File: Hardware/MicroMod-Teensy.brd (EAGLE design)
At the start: 22 x 22.8 mm, 80 parts, among them J1 MICROMOD-2222, Q1 20V/4.2A/52mΩ/1.4W, Q2 20V/0.2A/8MHz/1.2Ω/1Vth, U1 IMXRT1062DV10X10, U3 MKL02Z32VFG4, U4 W25QXX128MBIT-6X5, Y1 32.768kHz, Y2 24MHz

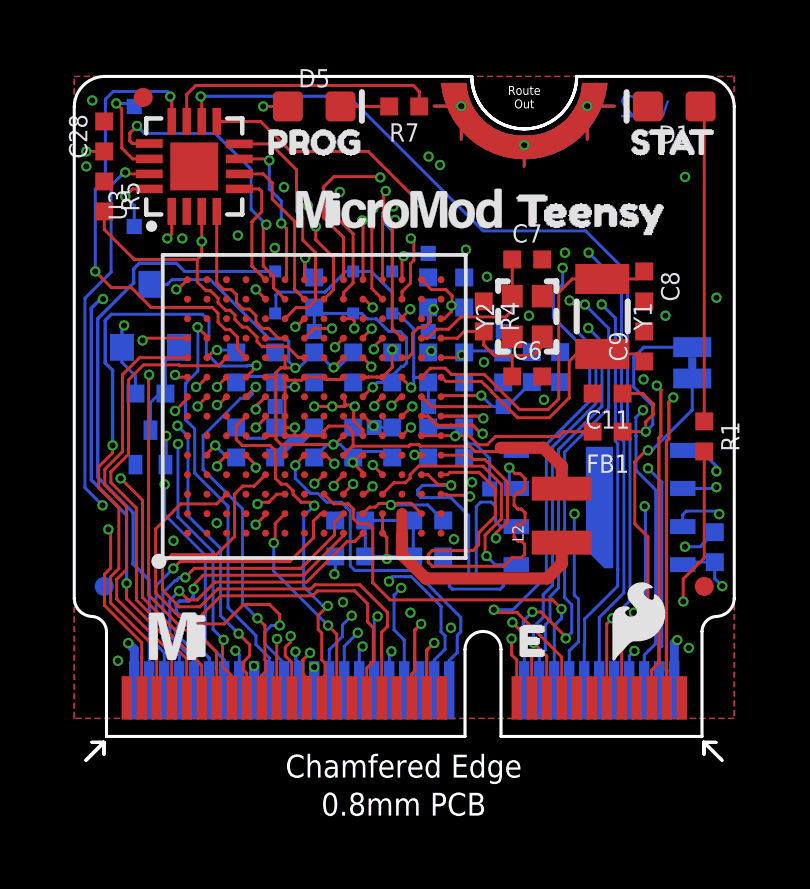
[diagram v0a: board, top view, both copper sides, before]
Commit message: Fix DAT2/DAT3, now correctly connected to B0_04 and B0_05.
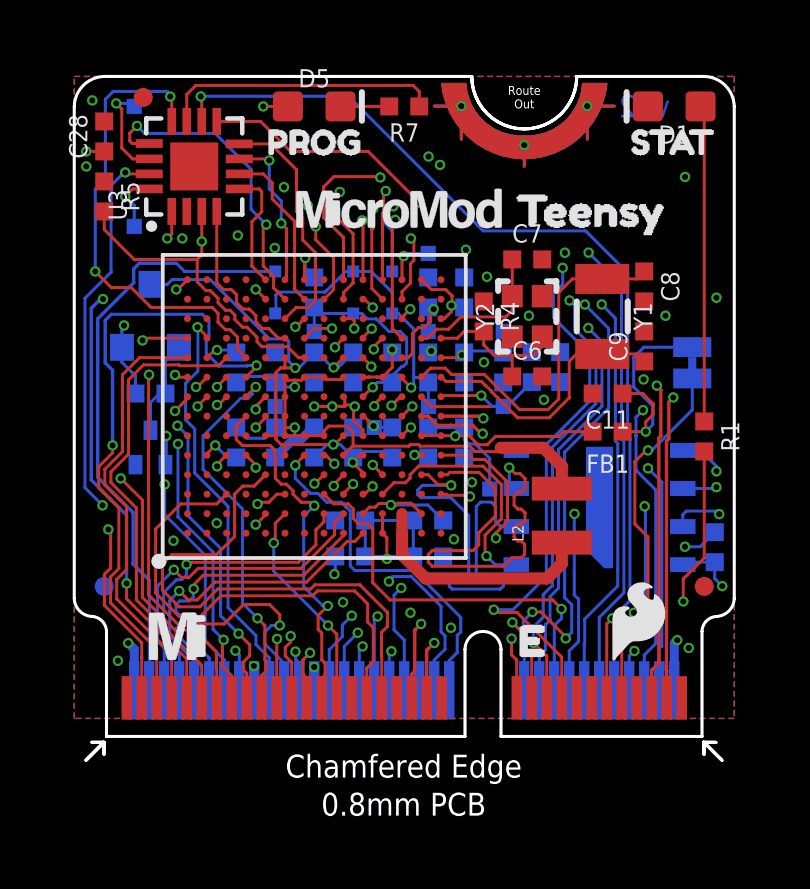
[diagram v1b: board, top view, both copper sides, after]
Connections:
- removed net 38/DAT3: J1.70, U1.H2
- removed net 39/DAT2: J1.68, U1.J2
- new net 38/DAT2: J1.68, U1.H2
- new net 39/DAT3: J1.70, U1.J2
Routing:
- net 39/DAT3: track 0.00 -> 11.2 mm, vias 0 -> 1
- net 39/DAT2: track 10.8 -> 0.00 mm, vias 1 -> 0
- net 38/DAT2: track 0.00 -> 10.6 mm, vias 0 -> 1
- net 38/DAT3: track 10.5 -> 0.00 mm, vias 1 -> 0
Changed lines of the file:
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@@
 <?xml version="1.0" encoding="utf-8"?>
 <!DOCTYPE eagle SYSTEM "eagle.dtd">
-<eagle version="9.6.0">
+<eagle version="9.6.2">
 <drawing>
 <settings>
@@
 <layer number="19" name="Unrouted" color="6" fill="1" visible="yes" active="yes"/>
 <layer number="20" name="Dimension" color="24" fill="1" visible="yes" active="yes"/>
-<layer number="21" name="tPlace" color="16" fill="1" visible="yes" active="yes"/>
+<layer number="21" name="tPlace" color="16" fill="1" visible="no" active="yes"/>
 <layer number="22" name="bPlace" color="14" fill="1" visible="yes" active="yes"/>
 <layer number="23" name="tOrigins" color="15" fill="1" visible="yes" active="yes"/>
@@
 <layer number="47" name="Measures" color="7" fill="1" visible="no" active="yes"/>
 <layer number="48" name="Document" color="7" fill="1" visible="no" active="yes"/>
-<layer number="49" name="Reference" color="7" fill="1" visible="no" active="yes"/>
+<layer number="49" name="Reference" color="7" fill="1" visible="yes" active="yes"/>
 <layer number="50" name="dxf" color="7" fill="1" visible="no" active="yes"/>
 <layer number="51" name="tDocu" color="6" fill="1" visible="yes" active="yes"/>
@@
 <wire x1="4.3" y1="5.36375" x2="7.65109375" y2="5.36375" width="0.1016" layer="1"/>
 <wire x1="7.65109375" y1="5.36375" x2="8.975" y2="6.68765625" width="0.1016" layer="1"/>
-<wire x1="4.31" y1="2.79" x2="4.01964375" y2="2.79" width="0.1143" layer="16"/>
-<wire x1="3.39535" y1="3.57535" x2="3.51" y2="3.69" width="0.1143" layer="16"/>
-<wire x1="4.05695" y1="3.69" x2="4.15695" y2="3.79" width="0.1143" layer="16"/>
-<wire x1="4.15695" y1="3.79" x2="4.15695" y2="3.94" width="0.1143" layer="16"/>
-<wire x1="4.15695" y1="3.94" x2="4.05695" y2="4.04" width="0.1143" layer="16"/>
-<wire x1="3.49535" y1="4.04" x2="3.39535" y2="4.14" width="0.1143" layer="16"/>
-<wire x1="3.39535" y1="4.3904" x2="3.51" y2="4.50505" width="0.1143" layer="16"/>
-<wire x1="3.51" y1="4.50505" x2="3.83874375" y2="4.50505" width="0.1143" layer="16"/>
-<wire x1="3.968" y1="4.63430625" x2="3.968" y2="4.895775" width="0.1143" layer="16"/>
-<wire x1="3.968" y1="4.63430625" x2="3.83874375" y2="4.50505" width="0.1143" layer="16"/>
-<wire x1="4.5" y1="2.6" x2="4.31" y2="2.79" width="0.1143" layer="16"/>
-<wire x1="4.01964375" y1="2.79" x2="3.39535" y2="3.41429375" width="0.1143" layer="16"/>
-<wire x1="3.39535" y1="3.41429375" x2="3.39535" y2="3.57535" width="0.1143" layer="16"/>
-<wire x1="3.51" y1="3.69" x2="4.05695" y2="3.69" width="0.1143" layer="16"/>
-<wire x1="4.05695" y1="4.04" x2="3.49535" y2="4.04" width="0.1143" layer="16"/>
-<wire x1="3.39535" y1="4.14" x2="3.39535" y2="4.3904" width="0.1143" layer="16"/>
+<wire x1="4.31" y1="2.79" x2="4.01964375" y2="2.79" width="0.1016" layer="16"/>
+<wire x1="3.39535" y1="3.57535" x2="3.51" y2="3.69" width="0.1016" layer="16"/>
+<wire x1="4.05695" y1="3.69" x2="4.15695" y2="3.79" width="0.1016" layer="16"/>
+<wire x1="4.15695" y1="3.79" x2="4.15695" y2="3.94" width="0.1016" layer="16"/>
+<wire x1="4.15695" y1="3.94" x2="4.05695" y2="4.04" width="0.1016" layer="16"/>
+<wire x1="3.49535" y1="4.04" x2="3.39535" y2="4.14" width="0.1016" layer="16"/>
+<wire x1="3.39535" y1="4.3904" x2="3.51" y2="4.50505" width="0.1016" layer="16"/>
+<wire x1="3.51" y1="4.50505" x2="3.83874375" y2="4.50505" width="0.1016" layer="16"/>
+<wire x1="3.968" y1="4.63430625" x2="3.968" y2="4.895775" width="0.1016" layer="16"/>
+<wire x1="3.968" y1="4.63430625" x2="3.83874375" y2="4.50505" width="0.1016" layer="16"/>
+<wire x1="4.5" y1="2.6" x2="4.31" y2="2.79" width="0.1016" layer="16"/>
+<wire x1="4.01964375" y1="2.79" x2="3.39535" y2="3.41429375" width="0.1016" layer="16"/>
+<wire x1="3.39535" y1="3.41429375" x2="3.39535" y2="3.57535" width="0.1016" layer="16"/>
+<wire x1="3.51" y1="3.69" x2="4.05695" y2="3.69" width="0.1016" layer="16"/>
+<wire x1="4.05695" y1="4.04" x2="3.49535" y2="4.04" width="0.1016" layer="16"/>
+<wire x1="3.39535" y1="4.14" x2="3.39535" y2="4.3904" width="0.1016" layer="16"/>
 <contactref element="J1" pad="64"/>
 <wire x1="4.5" y1="1.525" x2="4.5" y2="2.6" width="0.1016" layer="16"/>
@@
 <wire x1="8.65" y1="8.34" x2="8.4011375" y2="8.0911375" width="0.1016" layer="2"/>
 </signal>
-<signal name="38/DAT3">
-<contactref element="U1" pad="H2"/>
-<wire x1="8.325" y1="7.415" x2="8.22095" y2="7.415" width="0.1016" layer="1"/>
-<wire x1="8.22095" y1="7.415" x2="7.97465" y2="7.1687" width="0.1016" layer="1"/>
-<wire x1="7.97465" y1="6.61205" x2="7.97465" y2="7.1687" width="0.1016" layer="1"/>
-<via x="3.3" y="5.59" extent="1-16" drill="0.2"/>
-<wire x1="7.97465" y1="6.61205" x2="7.18355" y2="5.82095" width="0.1016" layer="1"/>
-<wire x1="3.3" y1="5.59" x2="3.53095" y2="5.82095" width="0.1016" layer="1"/>
-<wire x1="3.53095" y1="5.82095" x2="7.18355" y2="5.82095" width="0.1016" layer="1"/>
-<wire x1="3" y1="2.79" x2="2.7286" y2="3.0614" width="0.1016" layer="16"/>
-<wire x1="2.7286" y1="5.0186" x2="3.3" y2="5.59" width="0.1016" layer="16"/>
-<wire x1="2.7286" y1="3.0614" x2="2.7286" y2="5.0186" width="0.1016" layer="16"/>
+<signal name="39/DAT3">
 <contactref element="J1" pad="70"/>
-<wire x1="3" y1="1.525" x2="3" y2="2.79" width="0.1016" layer="16"/>
-</signal>
-<signal name="39/DAT2">
 <contactref element="U1" pad="J2"/>
 <wire x1="8.975" y1="7.415" x2="8.67535" y2="7.11535" width="0.1016" layer="1"/>
 <wire x1="8.67535" y1="7.11535" x2="8.67535" y2="6.7113" width="0.1016" layer="1"/>
 <wire x1="8.67535" y1="6.7113" x2="7.5564" y2="5.59235" width="0.1016" layer="1"/>
-<via x="3.7" y="5.29" extent="1-16" drill="0.2"/>
-<wire x1="3.7" y1="5.29" x2="4.00235" y2="5.59235" width="0.1016" layer="1"/>
-<wire x1="4.00235" y1="5.59235" x2="7.5564" y2="5.59235" width="0.1016" layer="1"/>
-<wire x1="3.5" y1="2.69" x2="2.9572" y2="3.2328" width="0.1016" layer="16"/>
-<wire x1="3.358625" y1="5.1813" x2="3.3985" y2="5.1813" width="0.1016" layer="16"/>
-<wire x1="3.3985" y1="5.1813" x2="3.5072" y2="5.29" width="0.1016" layer="16"/>
-<wire x1="2.9572" y1="3.2328" x2="2.9572" y2="4.779875" width="0.1016" layer="16"/>
-<wire x1="2.9572" y1="4.779875" x2="3.358625" y2="5.1813" width="0.1016" layer="16"/>
-<wire x1="3.5072" y1="5.29" x2="3.7" y2="5.29" width="0.1016" layer="16"/>
-<contactref element="J1" pad="68"/>
-<wire x1="3.5" y1="1.525" x2="3.5" y2="2.69" width="0.1016" layer="16"/>
+<via x="3.319" y="5.544" extent="1-16" drill="0.2"/>
+<wire x1="4.12935" y1="5.59235" x2="3.827" y2="5.29" width="0.1016" layer="1"/>
+<wire x1="3.827" y1="5.29" x2="3.573" y2="5.29" width="0.1016" layer="1"/>
+<wire x1="3.319" y1="5.544" x2="3.573" y2="5.29" width="0.1016" layer="1"/>
+<wire x1="4.12935" y1="5.59235" x2="7.5564" y2="5.59235" width="0.1016" layer="1"/>
+<wire x1="3" y1="1.525" x2="3" y2="2.93855625" width="0.1016" layer="16"/>
+<wire x1="3" y1="2.93855625" x2="2.7794" y2="3.15915625" width="0.1016" layer="16"/>
+<wire x1="2.7794" y1="3.15915625" x2="2.7794" y2="5.0044" width="0.1016" layer="16"/>
+<wire x1="2.7794" y1="5.0044" x2="3.319" y2="5.544" width="0.1016" layer="16"/>
 </signal>
 <signal name="N$31">
@@
 <wire x1="11.72218125" y1="9.7477" x2="12.4875875" y2="9.7477" width="0.1016" layer="2"/>
 </signal>
+<signal name="38/DAT2">
+<contactref element="U1" pad="H2"/>
+<contactref element="J1" pad="68"/>
+<wire x1="8.325" y1="7.415" x2="8.325" y2="7.1459875" width="0.1016" layer="1"/>
+<wire x1="8.0556" y1="6.37891875" x2="7.47223125" y2="5.79555" width="0.1016" layer="1"/>
+<wire x1="8.325" y1="7.1459875" x2="8.0556" y2="6.8765875" width="0.1016" layer="1"/>
+<wire x1="8.0556" y1="6.8765875" x2="8.0556" y2="6.37891875" width="0.1016" layer="1"/>
+<via x="3.74289375" y="5.72095" extent="1-16" drill="0.2"/>
+<wire x1="7.47223125" y1="5.79555" x2="3.91818125" y2="5.79555" width="0.1016" layer="1"/>
+<wire x1="3.91818125" y1="5.79555" x2="3.84358125" y2="5.72095" width="0.1016" layer="1"/>
+<wire x1="3.84358125" y1="5.72095" x2="3.74289375" y2="5.72095" width="0.1016" layer="1"/>
+<wire x1="3.74289375" y1="5.37618125" x2="3.74289375" y2="5.72095" width="0.1016" layer="16"/>
+<wire x1="3.74289375" y1="5.37618125" x2="3.5821125" y2="5.2154" width="0.1016" layer="16"/>
+<wire x1="2.9826" y1="4.7873125" x2="3.4106875" y2="5.2154" width="0.1016" layer="16"/>
+<wire x1="3.4106875" y1="5.2154" x2="3.5821125" y2="5.2154" width="0.1016" layer="16"/>
+<wire x1="2.9826" y1="3.243325" x2="2.9826" y2="4.7873125" width="0.1016" layer="16"/>
+<wire x1="3.5" y1="1.525" x2="3.5" y2="2.725925" width="0.1016" layer="16"/>
+<wire x1="3.5" y1="2.725925" x2="2.9826" y2="3.243325" width="0.1016" layer="16"/>
+</signal>
 </signals>

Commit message: Fix incorrect SDA/SCL1 board edge connector pinout
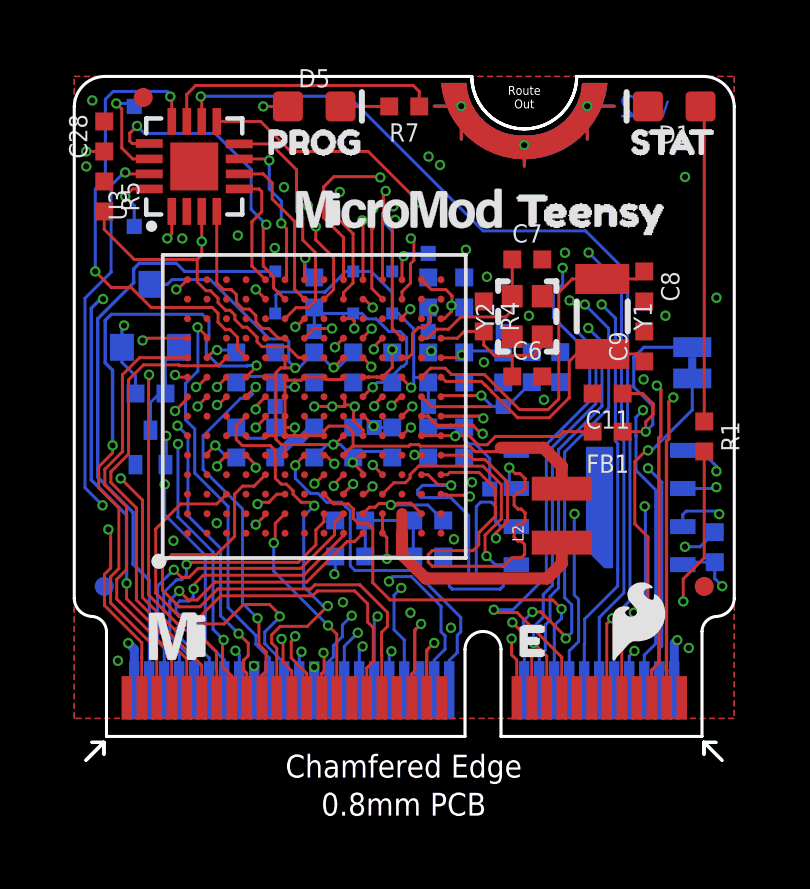
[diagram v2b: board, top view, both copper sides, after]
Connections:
- net BATT_VIN/22/A8: now also J1.49; no longer J1.51
- net CS/10: now also J1.55; no longer J1.49
- net SCL1/24/A10: now also J1.53; no longer J1.55
- net SDA1/25/A11: now also J1.51; no longer J1.53
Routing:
- net CS/10: track 12.3 -> 13.4 mm
- net BCLK/21/A7: track 20.7 -> 21.5 mm

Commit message: Update copper to v13. Add production files.
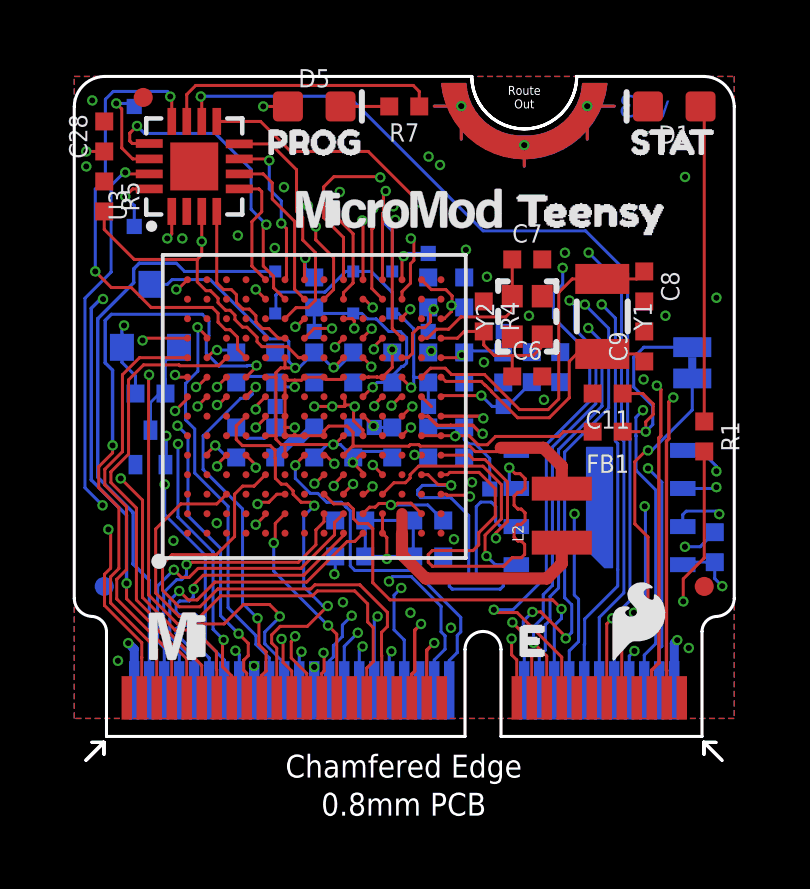
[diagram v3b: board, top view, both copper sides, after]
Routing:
- net GND: track 21.7 -> 19.5 mm
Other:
- board text added: "v13"
- board text removed: "v12"
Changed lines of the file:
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@@
 <?xml version="1.0" encoding="utf-8"?>
 <!DOCTYPE eagle SYSTEM "eagle.dtd">
-<eagle version="9.6.2">
+<eagle version="9.6.0">
 <drawing>
 <settings>
@@
 <setting verticaltext="up"/>
 </settings>
-<grid distance="1" unitdist="mm" unit="mm" style="lines" multiple="1" display="yes" altdistance="0.05" altunitdist="mm" altunit="mm"/>
+<grid distance="0.05" unitdist="inch" unit="inch" style="lines" multiple="1" display="yes" altdistance="0.005" altunitdist="inch" altunit="inch"/>
 <layers>
-<layer number="1" name="Top" color="4" fill="1" visible="yes" active="yes"/>
+<layer number="1" name="Top" color="4" fill="1" visible="no" active="yes"/>
 <layer number="2" name="Horz" color="1" fill="3" visible="no" active="yes"/>
 <layer number="15" name="Vert" color="4" fill="6" visible="no" active="yes"/>
@@
 <layer number="19" name="Unrouted" color="6" fill="1" visible="yes" active="yes"/>
 <layer number="20" name="Dimension" color="24" fill="1" visible="yes" active="yes"/>
-<layer number="21" name="tPlace" color="16" fill="1" visible="yes" active="yes"/>
-<layer number="22" name="bPlace" color="14" fill="1" visible="yes" active="yes"/>
-<layer number="23" name="tOrigins" color="15" fill="1" visible="yes" active="yes"/>
+<layer number="21" name="tPlace" color="16" fill="1" visible="no" active="yes"/>
+<layer number="22" name="bPlace" color="14" fill="1" visible="no" active="yes"/>
+<layer number="23" name="tOrigins" color="15" fill="1" visible="no" active="yes"/>
 <layer number="24" name="bOrigins" color="15" fill="1" visible="yes" active="yes"/>
 <layer number="25" name="tNames" color="7" fill="1" visible="no" active="yes"/>
@@
 <layer number="43" name="vRestrict" color="2" fill="10" visible="no" active="yes"/>
 <layer number="44" name="Drills" color="7" fill="1" visible="no" active="yes"/>
-<layer number="45" name="Holes" color="7" fill="1" visible="yes" active="yes"/>
+<layer number="45" name="Holes" color="7" fill="1" visible="no" active="yes"/>
 <layer number="46" name="Milling" color="3" fill="1" visible="no" active="yes"/>
 <layer number="47" name="Measures" color="7" fill="1" visible="no" active="yes"/>
 <layer number="48" name="Document" color="7" fill="1" visible="no" active="yes"/>
-<layer number="49" name="Reference" color="7" fill="1" visible="yes" active="yes"/>
+<layer number="49" name="Reference" color="7" fill="1" visible="no" active="yes"/>
 <layer number="50" name="dxf" color="7" fill="1" visible="no" active="yes"/>
-<layer number="51" name="tDocu" color="6" fill="1" visible="yes" active="yes"/>
+<layer number="51" name="tDocu" color="6" fill="1" visible="no" active="yes"/>
 <layer number="52" name="bDocu" color="7" fill="1" visible="no" active="yes"/>
 <layer number="91" name="Nets" color="2" fill="1" visible="no" active="no"/>
@@
 <wire x1="22" y1="18.99" x2="0" y2="18.99" width="0.1016" layer="51"/>
 <wire x1="0" y1="18.99" x2="0" y2="4.99" width="0.1016" layer="51"/>
-<text x="19" y="21" size="0.75" layer="16" font="vector" ratio="20" rot="MR0" align="center">v12</text>
+<text x="19" y="21" size="0.75" layer="16" font="vector" ratio="20" rot="MR0" align="center">v13</text>
 <text x="30.35" y="31.67" size="1.778" layer="51" font="vector" ratio="15">0.8mm PCB
 45 degree chamfered edge
@@
 <wire x1="11.3429" y1="9.3749" x2="11.3528" y2="9.365" width="0.1016" layer="1"/>
 <via x="11.3429" y="9.3749" extent="1-16" drill="0.2"/>
-<wire x1="12.8" y1="11.79" x2="13" y2="11.79" width="0.1016" layer="16"/>
 <via x="13.056" y="16.213" extent="1-16" drill="0.2"/>
 <via x="13.756" y="15.313" extent="1-16" drill="0.2"/>
@@
 <wire x1="5.1" y1="9.29" x2="4.7" y2="9.69" width="0.1016" layer="16"/>
 <wire x1="11.575" y1="11.315" x2="11.9071" y2="10.9829" width="0.1016" layer="1"/>
-<wire x1="11.9071" y1="10.9829" x2="13.86459375" y2="10.9829" width="0.1016" layer="1"/>
 <wire x1="10.55546875" y1="7.7051" x2="10.71998125" y2="7.7051" width="0.1016" layer="1"/>
 <wire x1="10.71998125" y1="7.7051" x2="10.77998125" y2="7.7651" width="0.1016" layer="1"/>

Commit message: Remove traces from beneath xtals.
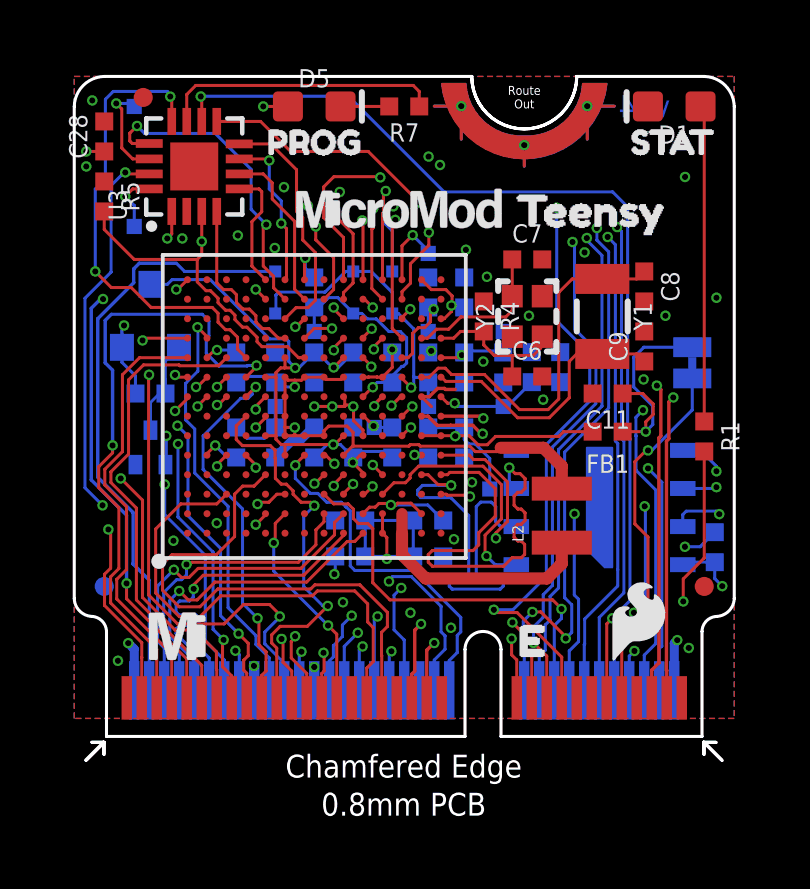
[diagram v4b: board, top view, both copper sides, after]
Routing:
- net RX1/16/A2: track 21.7 -> 35.5 mm
- net TX1/17/A3: track 25.4 -> 32.7 mm
- net SDA/18/A4: track 26.6 -> 33.7 mm
- net A0/14: track 19.2 -> 15.1 mm
- net SCL/19/A5: track 25.9 -> 29.9 mm
- net RX0/0: track 25.2 -> 27.8 mm
- net PROGRAM: track 32.0 -> 33.3 mm
- net GND: track 19.5 -> 20.8 mm
- net MCLK/23/A9: track 25.4 -> 26.6 mm
- net TX0/1: track 28.4 -> 29.5 mm
- net 32KHZ_TEST: track 1.67 -> 2.46 mm
- net 3.3V_CONTROLLED: track 29.0 -> 28.4 mm
- added copper zone on layer 2, net GND
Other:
- board text added: "v14"
- board text removed: "v13"
